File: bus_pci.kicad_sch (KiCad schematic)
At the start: 33 parts, among them U1 24C16, U11 S5933_PQ160

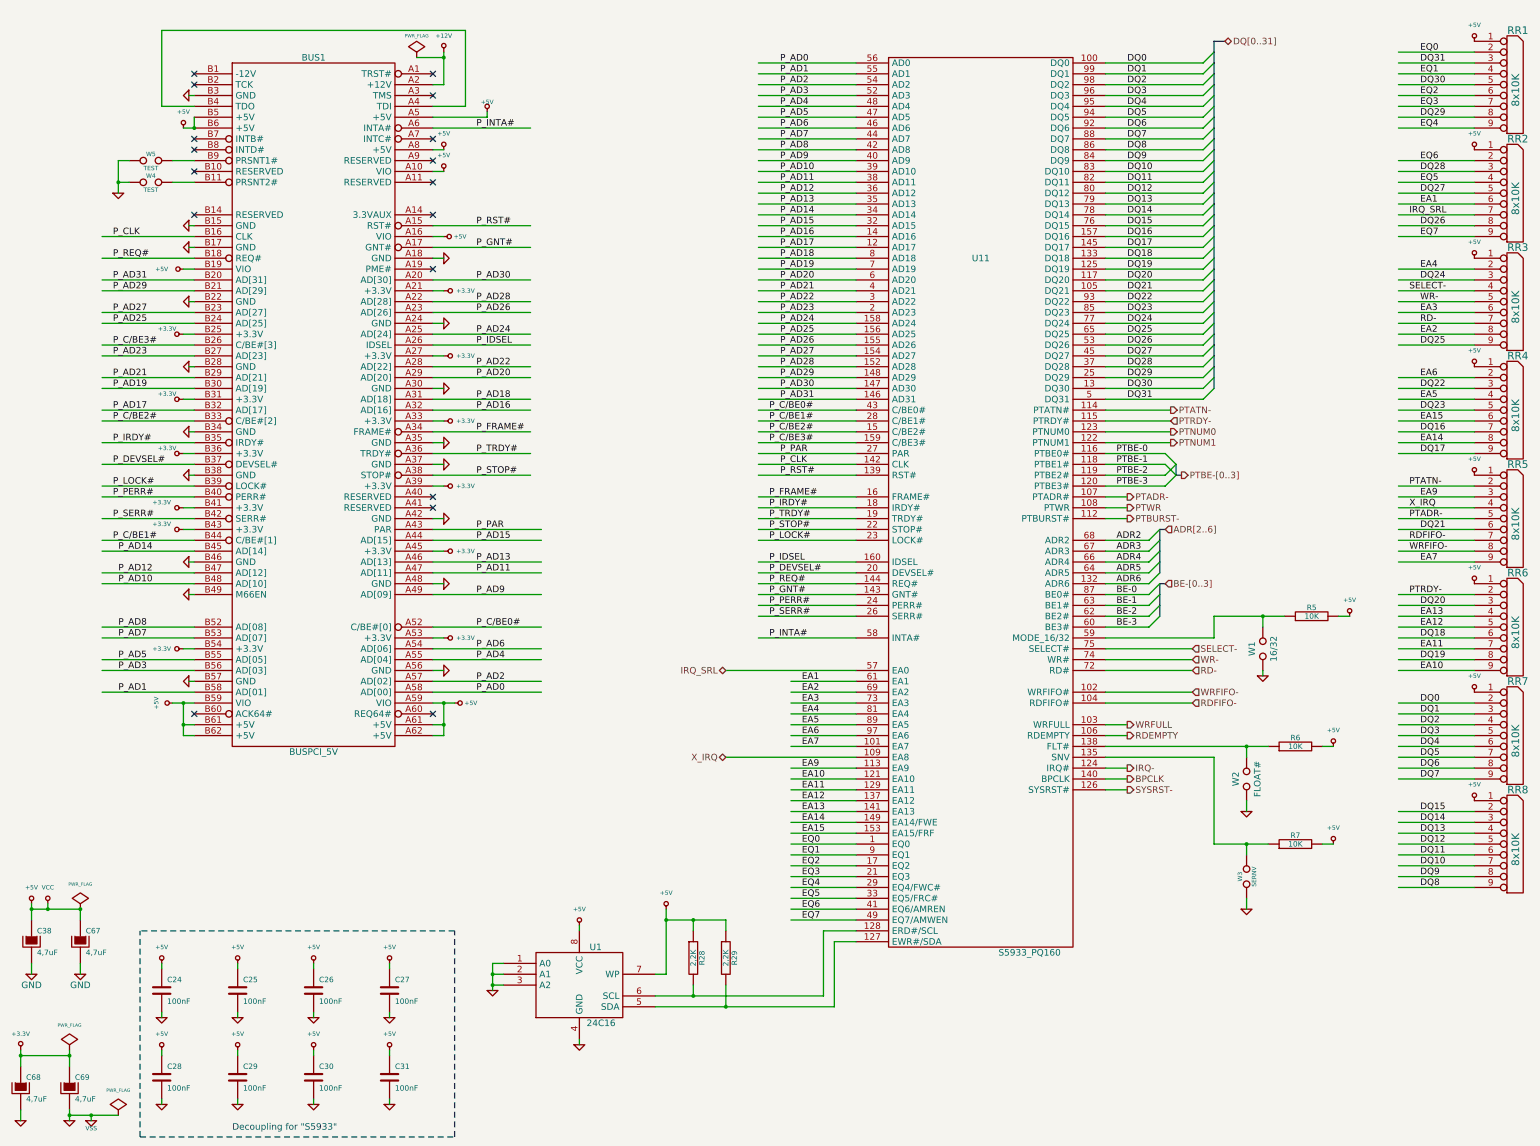
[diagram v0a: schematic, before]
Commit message: update to kicad 9
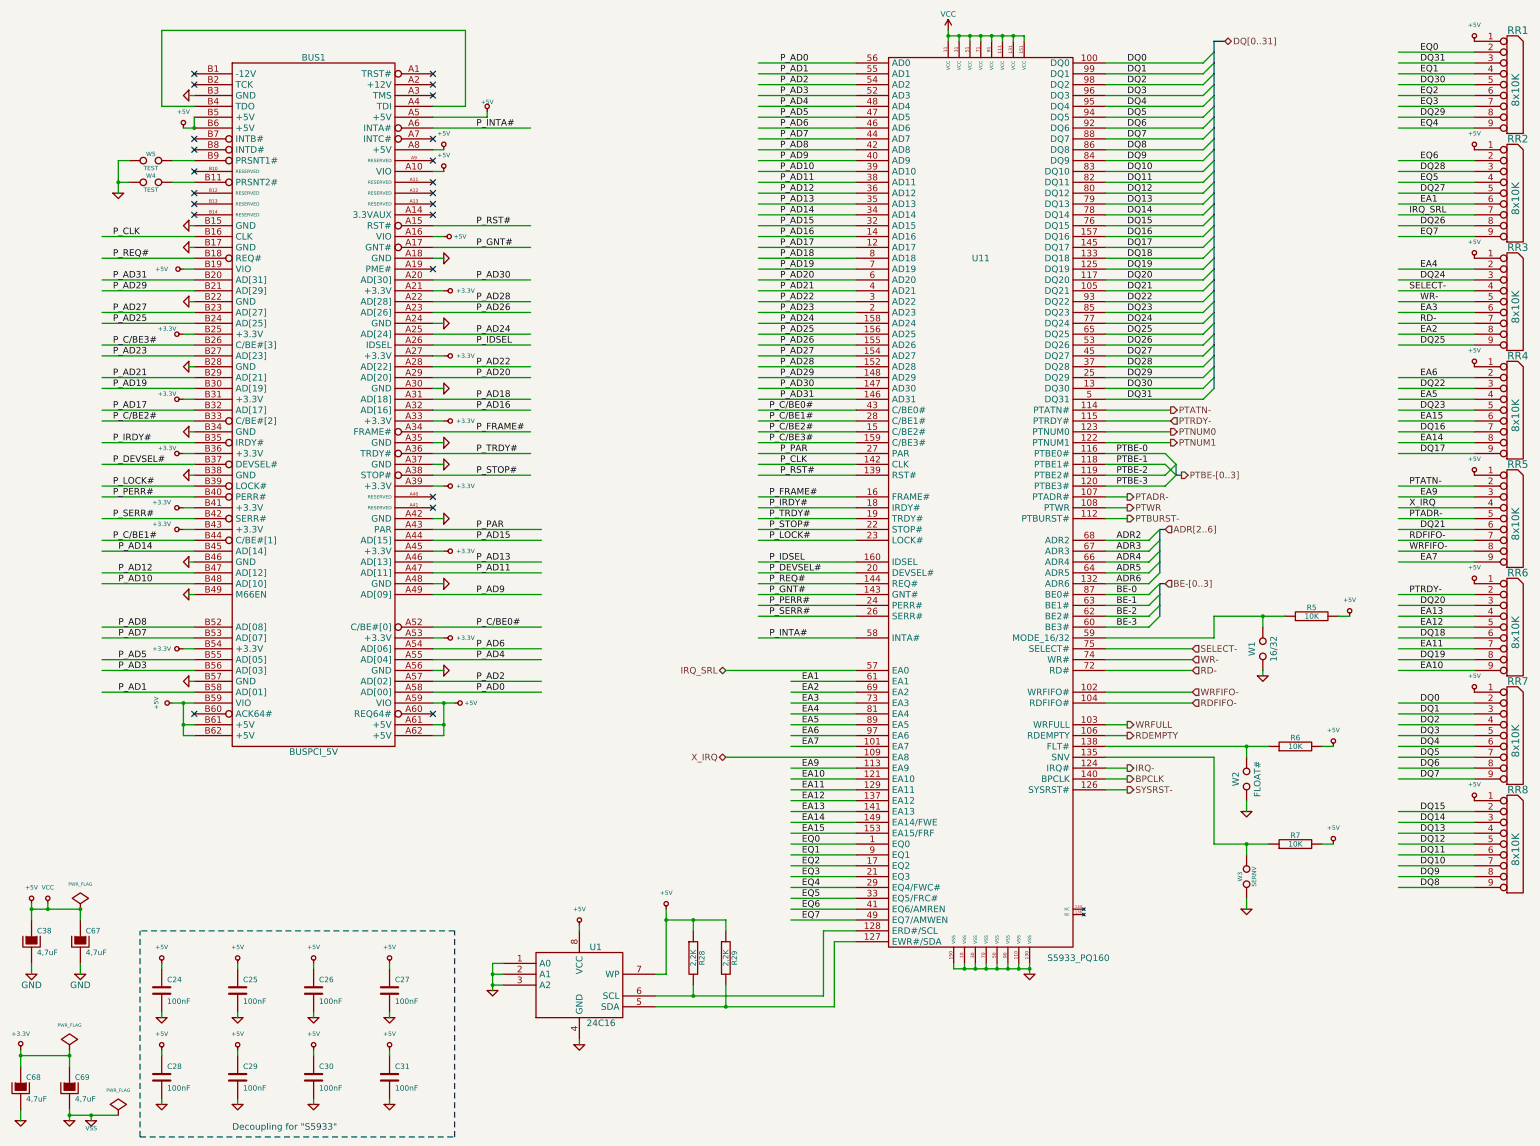
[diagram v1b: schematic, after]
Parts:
- BUS1: footprint Connectors:BUSPCI -> footprints:BUSPCI
- C24, C25, C26, C27, C28, C29, C30, C31, C38, C67, C68, C69, R28, R29, R5, R6, R7: footprint Resistor_SMD:R_1206_3216Metric_Pad1.24x1.80mm_HandSolder -> Resistor_SMD:R_1206_3216Metric_Pad1.30x1.75mm_HandSolder
- W1, W2, W3: footprint Connectors:GS2 -> footprints:SolderJumper-2_P1.3mm_Open_Pad1.0x1.5mm; now left out of the parts list
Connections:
- net +12V: no longer names the net of BUS1.A2 (+12V)
- no-connect marks 17 -> 22
